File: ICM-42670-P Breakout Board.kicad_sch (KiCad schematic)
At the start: 10 parts, among them J2 Conn_01x09_Pin, U1 ICM-42670-P, U2 MCP1700x-330xxTT

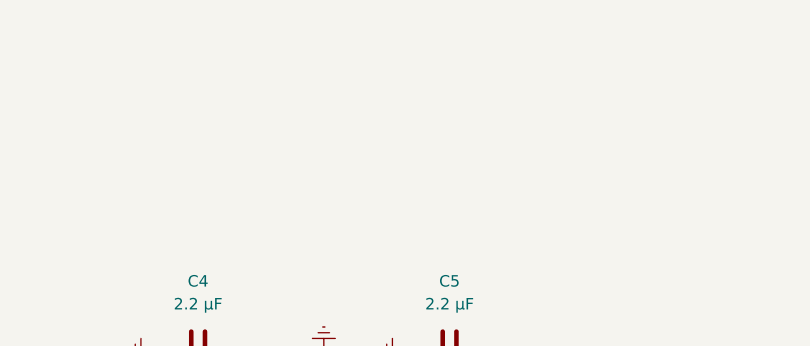
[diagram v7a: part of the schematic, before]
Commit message: Add Indicator LED
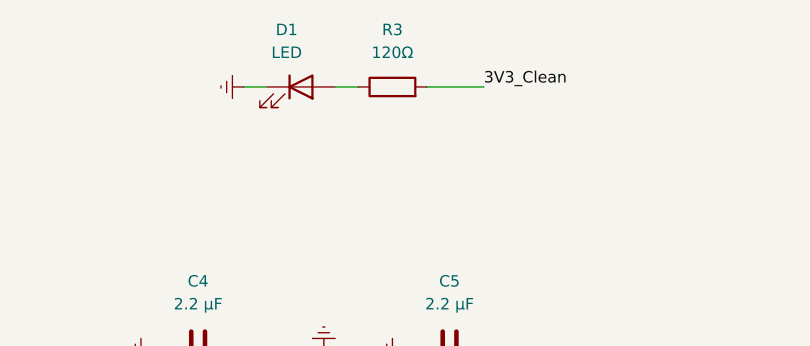
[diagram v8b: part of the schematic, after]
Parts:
- added D1: LED, LED_SMD:LED_0603_1608Metric, symbol Device:LED
- added R3: 120Ω, Resistor_SMD:R_0402_1005Metric, symbol Device:R
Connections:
- net 3V3_Clean: now also R3.2
- net GND: now also D1.1 (K)
- new net: D1.2 (A), R3.1
